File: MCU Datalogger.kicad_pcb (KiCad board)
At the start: 2 copper layers, 52.8 x 34.3 mm, 29 parts, among them J1 Conn_01x04_Pin, J2 Conn_01x09_Pin, J3 Conn_01x04_Pin, J4 Conn_02x03_Odd_Even, U1 24LC1025, U2 DS1337S_, U3 24LC1025, U4 ATMEGA328P-AU, Y1 32.768 KHz, Y2 16 MHz

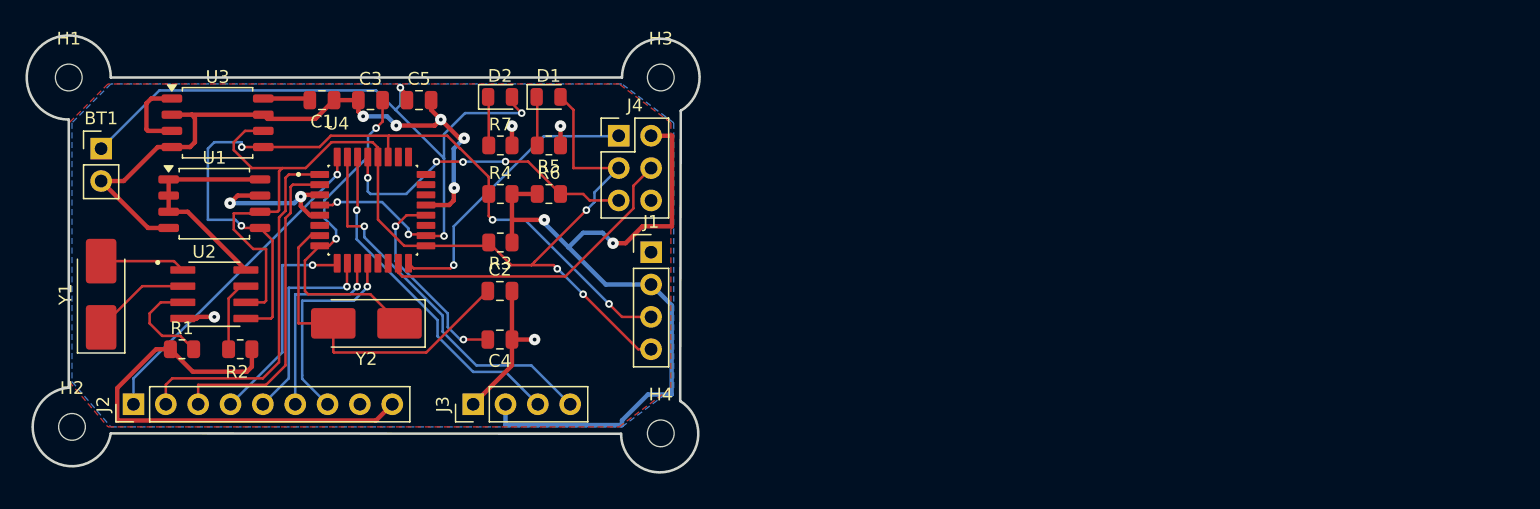
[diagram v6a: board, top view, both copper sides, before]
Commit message: Improved routing. Arranged values and ref. texts
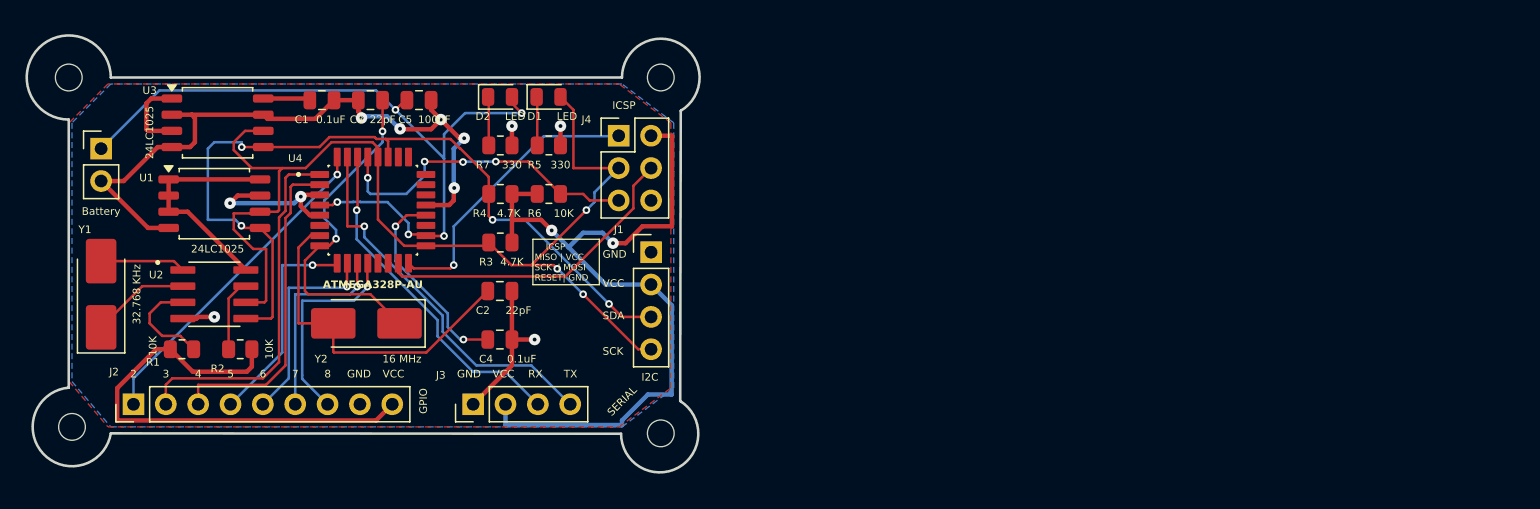
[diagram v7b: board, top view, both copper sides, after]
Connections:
- BT1 pad 1: Net-(BT1-+) -> /VCC
- C5 pad 1: Net-(BT1-+) -> /VCC
- D2 pad 2: Net-(BT1-+) -> /VCC
- U4 pad 18: Net-(BT1-+) -> /VCC
- U4 pad 4: Net-(BT1-+) -> /VCC
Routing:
- net Net-(BT1-+): track 61.7 -> 0.00 mm, vias 5 -> 0
- net /VCC: track 128.8 -> 188.7 mm, vias 2 -> 7
- net /RESET: track 24.9 -> 25.5 mm
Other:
- board text added: "2"
- board text added: "3"
- board text added: "4"
- board text added: "5"
- board text added: "6"
- board text added: "7"
- board text added: "8"
- board text added: "GND"
- board text added: "GPIO"
- board text added: "I2C"
- board text added: "ICSP"
- board text added: "ICSP MISO | VCC SCK | MOSI RESET| GND"
- board text added: "RX"
- board text added: "SCK"
- board text added: "SDA"
- board text added: "SERIAL"
- board text added: "TX"
- board text added: "VCC"

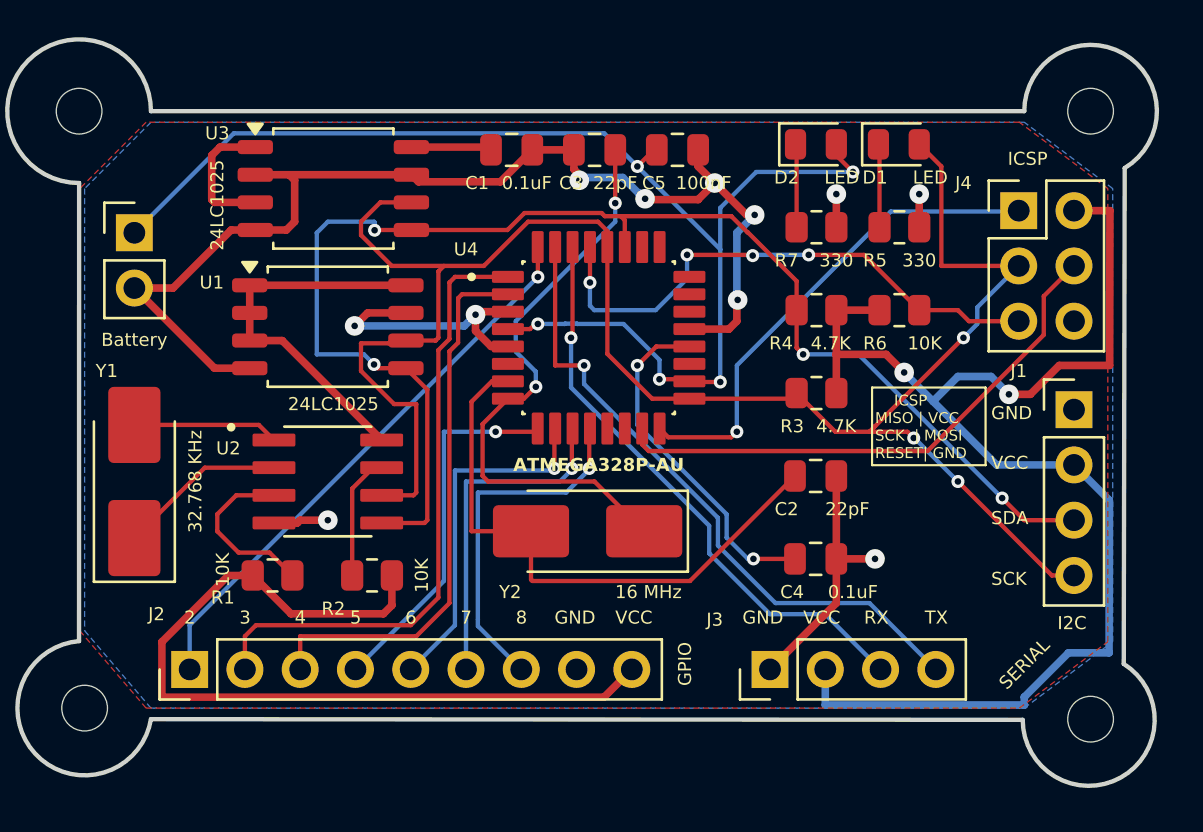
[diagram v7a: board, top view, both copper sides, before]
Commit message: Fixed outstanding issues. Added information on Back Silkscreen
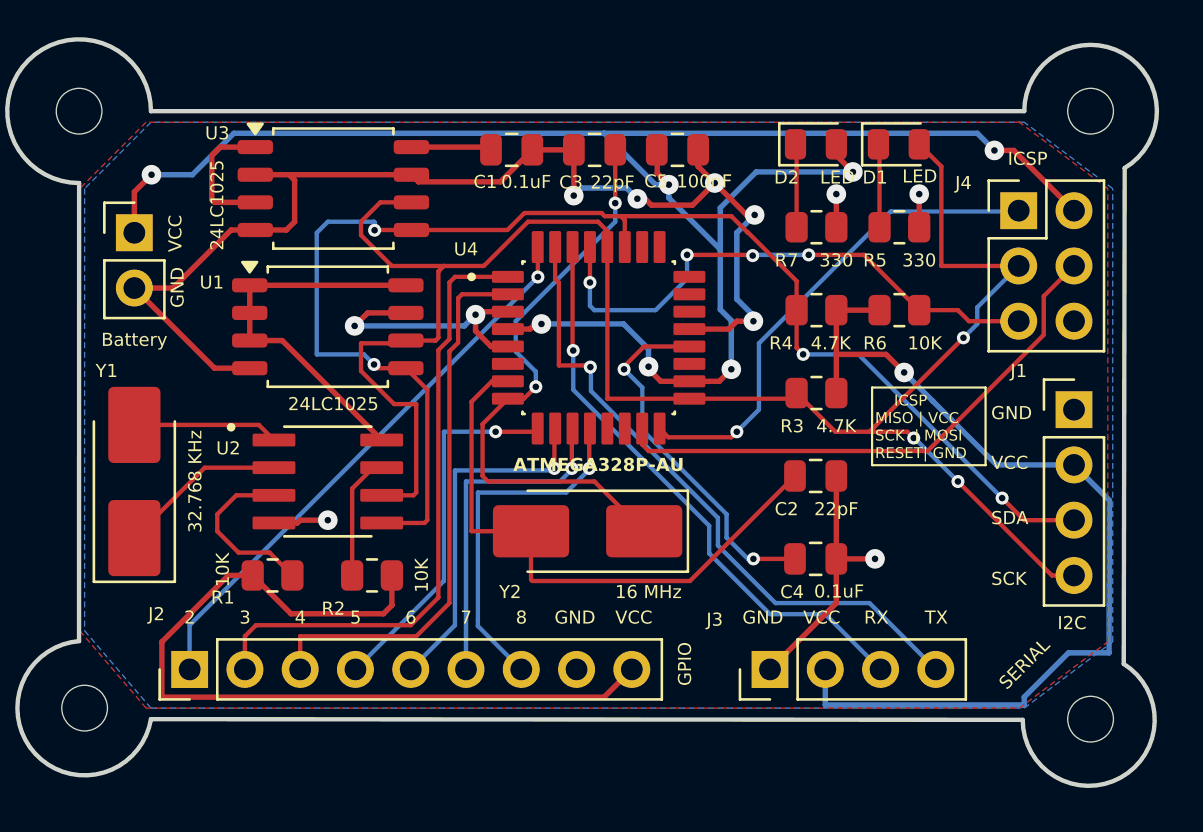
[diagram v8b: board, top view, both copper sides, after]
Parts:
- added REF**: KiCad-Logo2_5mm_SilkScreen, Symbol:KiCad-Logo2_5mm_SilkScreen, B.Cu at (68.5, 61.5)
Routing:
- net /VCC: track 188.7 -> 196.0 mm, vias 7 -> 8
- net GND: track 83.9 -> 85.9 mm
- net /SCK: track 85.0 -> 86.2 mm
- net Net-(U4-AREF): track 15.9 -> 16.7 mm
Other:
- board text added: "- 2Mbit EEPROM - RTC - I2C, SPI, GPIOs"
- board text added: "Datalogger with ATMega328P."
- board text added: "Demo project by Mithun"
